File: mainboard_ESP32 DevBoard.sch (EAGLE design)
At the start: 46 parts, among them IC1 OP-AMP-2-LONG, IC3 74HC08N, K1 AQH213, X1 JST-XH-02-PIN-LONG-PAD, X2 JST-XH-04-PIN-LONG-PAD, X3 1751248, X4 1751248, X5 JST-XH-04-PIN-LONG-PAD, X6 1751248

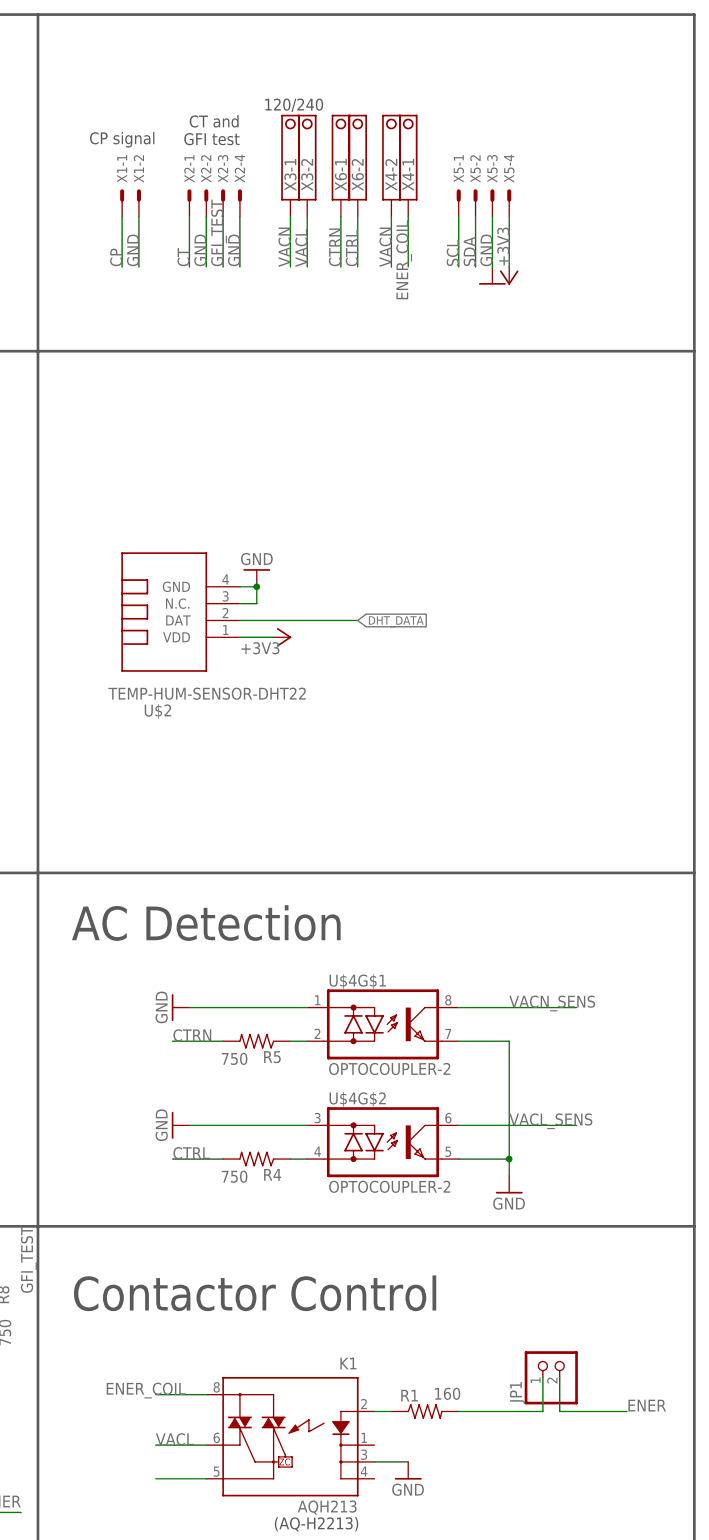
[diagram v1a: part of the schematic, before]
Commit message: Swapped ac headers for one big one and added dedicated earth terminal
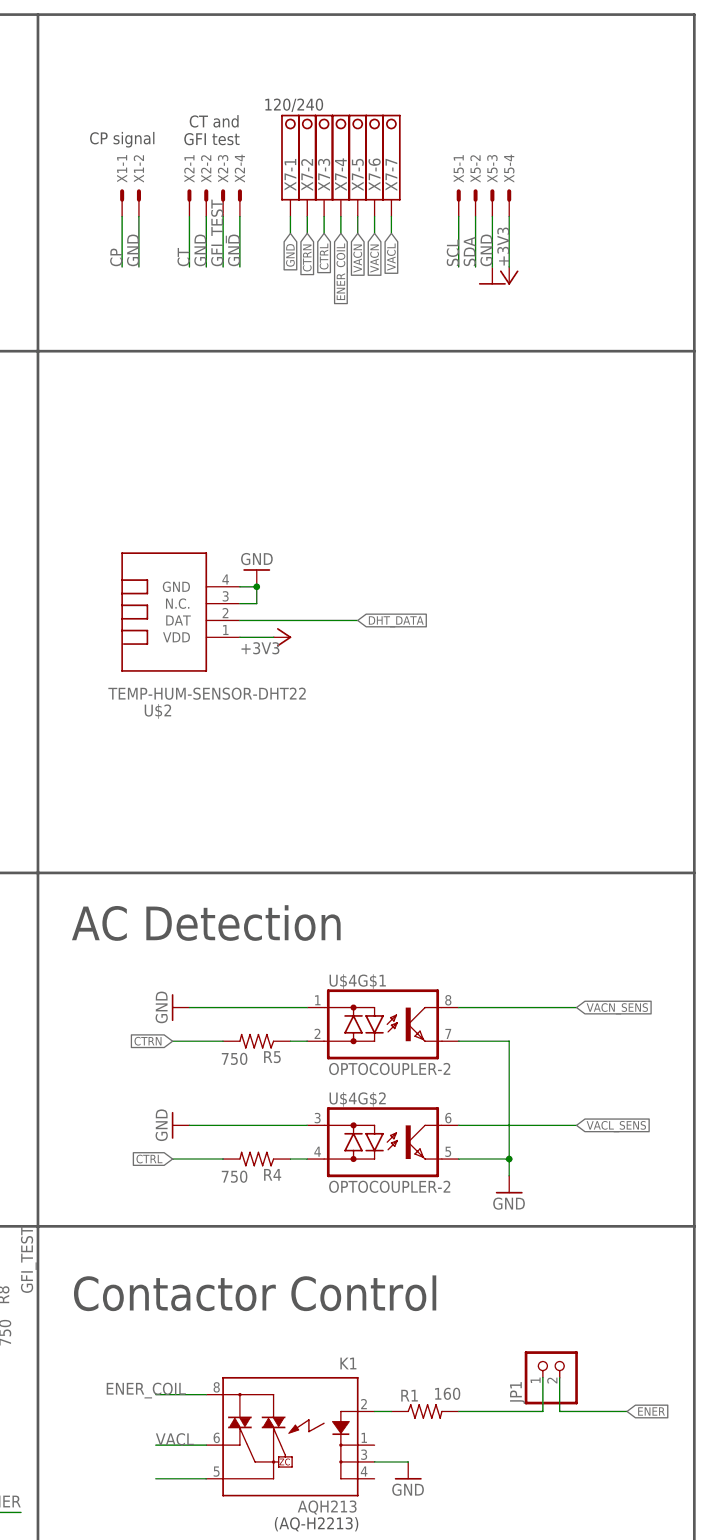
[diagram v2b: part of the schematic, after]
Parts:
- removed X3, X4, X6: 1751248, con-phoenix-350:1751248
- added X7: 1751293, con-phoenix-350:1751293
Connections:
- net CTRL: now also X7-3.K; no longer X6-2.K
- net CTRN: now also X7-2.K; no longer X6-1.K
- net ENER_COIL: now also X7-4.K; no longer X4-1.K
- net GND: now also X7-1.K
- net VACL: now also X7-7.K; no longer X3-2.K
- net VACN: now also X7-5.K, X7-6.K; no longer X3-1.K, X4-2.K
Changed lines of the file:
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@@
 <part name="X1" library="Rembrandt Electronics - JST XH Connectors v1-0" deviceset="JST-XH-02-PIN" device="-LONG-PAD"/>
 <part name="X2" library="Rembrandt Electronics - JST XH Connectors v1-0" deviceset="JST-XH-04-PIN" device="-LONG-PAD"/>
-<part name="X3" library="con-phoenix-350" library_urn="urn:adsk.eagle:library:174" deviceset="1751248" device="" package3d_urn="urn:adsk.eagle:package:9395/1"/>
-<part name="X4" library="con-phoenix-350" library_urn="urn:adsk.eagle:library:174" deviceset="1751248" device="" package3d_urn="urn:adsk.eagle:package:9395/1"/>
 <part name="R2" library="Passive" deviceset="RESISTOR" device="L" value="560"/>
 <part name="GND3" library="supply1" library_urn="urn:adsk.eagle:library:371" deviceset="GND" device=""/>
@@
 <part name="GND17" library="supply1" library_urn="urn:adsk.eagle:library:371" deviceset="GND" device=""/>
 <part name="GND18" library="supply1" library_urn="urn:adsk.eagle:library:371" deviceset="GND" device=""/>
-<part name="X6" library="con-phoenix-350" library_urn="urn:adsk.eagle:library:174" deviceset="1751248" device="" package3d_urn="urn:adsk.eagle:package:9395/1"/>
+<part name="X7" library="con-phoenix-350" library_urn="urn:adsk.eagle:library:174" deviceset="1751293" device="" package3d_urn="urn:adsk.eagle:package:9398/1"/>
 </parts>
 <sheets>
@@
 <attribute name="NAME" x="160.782" y="129.54" size="1.524" layer="95" rot="R90"/>
 </instance>
-<instance part="X3" gate="-1" x="167.64" y="127" smashed="yes" rot="R90">
-<attribute name="NAME" x="168.529" y="128.27" size="1.778" layer="95" rot="R90"/>
-</instance>
-<instance part="X3" gate="-2" x="170.18" y="127" smashed="yes" rot="R90">
-<attribute name="NAME" x="171.069" y="128.27" size="1.778" layer="95" rot="R90"/>
-</instance>
-<instance part="X4" gate="-1" x="185.42" y="127" smashed="yes" rot="R90">
-<attribute name="NAME" x="186.309" y="128.27" size="1.778" layer="95" rot="R90"/>
-</instance>
-<instance part="X4" gate="-2" x="182.88" y="127" smashed="yes" rot="R90">
-<attribute name="NAME" x="183.769" y="128.27" size="1.778" layer="95" rot="R90"/>
-</instance>
 <instance part="R2" gate="G$1" x="43.18" y="-83.82" smashed="yes" rot="R180">
 <attribute name="NAME" x="49.53" y="-80.2386" size="1.778" layer="95" rot="R180"/>
@@
 <attribute name="VALUE" x="198.12" y="-25.4" size="1.778" layer="96"/>
 </instance>
-<instance part="X6" gate="-1" x="175.26" y="127" smashed="yes" rot="R90">
+<instance part="X7" gate="-1" x="167.64" y="127" smashed="yes" rot="R90">
+<attribute name="NAME" x="168.529" y="128.27" size="1.778" layer="95" rot="R90"/>
+</instance>
+<instance part="X7" gate="-2" x="170.18" y="127" smashed="yes" rot="R90">
+<attribute name="NAME" x="171.069" y="128.27" size="1.778" layer="95" rot="R90"/>
+</instance>
+<instance part="X7" gate="-3" x="172.72" y="127" smashed="yes" rot="R90">
+<attribute name="NAME" x="173.609" y="128.27" size="1.778" layer="95" rot="R90"/>
+</instance>
+<instance part="X7" gate="-4" x="175.26" y="127" smashed="yes" rot="R90">
 <attribute name="NAME" x="176.149" y="128.27" size="1.778" layer="95" rot="R90"/>
 </instance>
-<instance part="X6" gate="-2" x="177.8" y="127" smashed="yes" rot="R90">
+<instance part="X7" gate="-5" x="177.8" y="127" smashed="yes" rot="R90">
 <attribute name="NAME" x="178.689" y="128.27" size="1.778" layer="95" rot="R90"/>
+</instance>
+<instance part="X7" gate="-6" x="180.34" y="127" smashed="yes" rot="R90">
+<attribute name="NAME" x="181.229" y="128.27" size="1.778" layer="95" rot="R90"/>
+</instance>
+<instance part="X7" gate="-7" x="182.88" y="127" smashed="yes" rot="R90">
+<attribute name="NAME" x="183.769" y="128.27" size="1.778" layer="95" rot="R90"/>
 </instance>
 </instances>
@@
 <junction x="200.66" y="-17.78"/>
 </segment>
+<segment>
+<pinref part="X7" gate="-1" pin="K"/>
+<wire x1="167.64" y1="124.46" x2="167.64" y2="121.92" width="0.1524" layer="91"/>
+<label x="167.64" y="121.92" size="1.27" layer="95" rot="R270" xref="yes"/>
+</segment>
 </net>
 <net name="+3V3" class="0">
@@
 <wire x1="208.28" y1="-50.8" x2="208.28" y2="-55.88" width="0.1524" layer="91"/>
 <wire x1="208.28" y1="-55.88" x2="218.44" y2="-55.88" width="0.1524" layer="91"/>
-<label x="218.44" y="-55.88" size="1.778" layer="95"/>
+<label x="218.44" y="-55.88" size="1.27" layer="95" xref="yes"/>
 </segment>
 </net>
@@
 </segment>
 <segment>
-<pinref part="X4" gate="-1" pin="K"/>
-<wire x1="185.42" y1="124.46" x2="185.42" y2="116.84" width="0.1524" layer="91"/>
-<label x="185.42" y="111.76" size="1.778" layer="95" rot="R90"/>
+<pinref part="X7" gate="-4" pin="K"/>
+<wire x1="175.26" y1="121.92" x2="175.26" y2="124.46" width="0.1524" layer="91"/>
+<label x="175.26" y="121.92" size="1.27" layer="95" rot="R270" xref="yes"/>
 </segment>
 </net>
@@
 </segment>
 <segment>
-<pinref part="X3" gate="-2" pin="K"/>
-<wire x1="170.18" y1="124.46" x2="170.18" y2="116.84" width="0.1524" layer="91"/>
-<label x="170.18" y="116.84" size="1.778" layer="95" rot="R90"/>
+<pinref part="X7" gate="-7" pin="K"/>
+<wire x1="182.88" y1="121.92" x2="182.88" y2="124.46" width="0.1524" layer="91"/>
+<label x="182.88" y="121.92" size="1.27" layer="95" rot="R270" xref="yes"/>
 </segment>
 </net>
@@
 </segment>
 <segment>
-<pinref part="X3" gate="-1" pin="K"/>
-<wire x1="167.64" y1="124.46" x2="167.64" y2="116.84" width="0.1524" layer="91"/>
-<label x="167.64" y="116.84" size="1.778" layer="95" rot="R90"/>
-</segment>
-<segment>
-<pinref part="X4" gate="-2" pin="K"/>
-<wire x1="182.88" y1="124.46" x2="182.88" y2="116.84" width="0.1524" layer="91"/>
-<label x="182.88" y="116.84" size="1.778" layer="95" rot="R90"/>
+<pinref part="X7" gate="-5" pin="K"/>
+<wire x1="177.8" y1="121.92" x2="177.8" y2="124.46" width="0.1524" layer="91"/>
+<label x="177.8" y="121.92" size="1.27" layer="95" rot="R270" xref="yes"/>
+</segment>
+<segment>
+<pinref part="X7" gate="-6" pin="K"/>
+<wire x1="180.34" y1="121.92" x2="180.34" y2="124.46" width="0.1524" layer="91"/>
+<label x="180.34" y="121.92" size="1.27" layer="95" rot="R270" xref="yes"/>
 </segment>
 </net>
@@
 <pinref part="U$4" gate="G$1" pin="C"/>
 <wire x1="193.04" y1="5.08" x2="210.82" y2="5.08" width="0.1524" layer="91"/>
-<label x="200.66" y="5.08" size="1.778" layer="95"/>
+<label x="210.82" y="5.08" size="1.27" layer="95" xref="yes"/>
 </segment>
 <segment>
@@
 <pinref part="U$4" gate="G$2" pin="C"/>
 <wire x1="193.04" y1="-12.7" x2="210.82" y2="-12.7" width="0.1524" layer="91"/>
-<label x="200.66" y="-12.7" size="1.778" layer="95"/>
+<label x="210.82" y="-12.7" size="1.27" layer="95" xref="yes"/>
 </segment>
 <segment>
@@
 <net name="CTRN" class="1">
 <segment>
-<pinref part="X6" gate="-1" pin="K"/>
-<wire x1="175.26" y1="124.46" x2="175.26" y2="116.84" width="0.1524" layer="91"/>
-<label x="175.26" y="116.84" size="1.778" layer="95" rot="R90"/>
-</segment>
-<segment>
 <pinref part="R5" gate="G$1" pin="2"/>
 <wire x1="157.48" y1="0" x2="149.86" y2="0" width="0.1524" layer="91"/>
-<label x="149.86" y="0" size="1.778" layer="95"/>
+<label x="149.86" y="0" size="1.27" layer="95" rot="R180" xref="yes"/>
+</segment>
+<segment>
+<pinref part="X7" gate="-2" pin="K"/>
+<wire x1="170.18" y1="121.92" x2="170.18" y2="124.46" width="0.1524" layer="91"/>
+<label x="170.18" y="121.92" size="1.27" layer="95" rot="R270" xref="yes"/>
 </segment>
 </net>
 <net name="CTRL" class="1">
-<segment>
-<pinref part="X6" gate="-2" pin="K"/>
-<wire x1="177.8" y1="124.46" x2="177.8" y2="116.84" width="0.1524" layer="91"/>
-<label x="177.8" y="116.84" size="1.778" layer="95" rot="R90"/>
-</segment>
 <segment>
 <pinref part="R4" gate="G$1" pin="2"/>
 <wire x1="157.48" y1="-17.78" x2="149.86" y2="-17.78" width="0.1524" layer="91"/>
-<label x="149.86" y="-17.78" size="1.778" layer="95"/>
-</segment>
-</net>
+<label x="149.86" y="-17.78" size="1.27" layer="95" rot="R180" xref="yes"/>
+</segment>
+<segment>
+<pinref part="X7" gate="-3" pin="K"/>
+<wire x1="172.72" y1="121.92" x2="172.72" y2="124.46" width="0.1524" layer="91"/>
+<label x="172.72" y="121.92" size="1.27" layer="95" rot="R270" xref="yes"/>
+</segment>
+</net>
